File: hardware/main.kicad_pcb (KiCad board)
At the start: 2 copper layers, 5 parts, among them U1 SN74LVC245APW, U2 SN74LVC245APW, U3 SN74LVC245APW, U4 Z084000xP

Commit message: update pcb files
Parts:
- moved A1 58.3 mm to (62.6, 142.5), turned to -90 degrees
- moved U3 47.1 mm to (50.6, 118.2), turned to 180 degrees
- moved U1 46.1 mm to (78.0, 118.2)
- moved U2 43.9 mm to (64.5, 118.2)
- moved U4 32.4 mm to (85.5, 87.0), turned to -90 degrees
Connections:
- A1 pad 31: unconnected-(A1-GPIO26_ADC0-Pad31) -> IORQ
- A1 pad 32: KEYB -> WR
- A1 pad 34: unconnected-(A1-GPIO28_ADC2-Pad34)_1 -> KEYB
- U4 pad 20: unconnected-(U4-~{IORQ}-Pad20) -> IORQ
- U4 pad 22: unconnected-(U4-~{WR}-Pad22) -> WR
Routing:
- net +5V: track 0.00 -> 129.5 mm, vias 0 -> 4
- net CLK: track 0.00 -> 83.6 mm, vias 0 -> 1
- net IORQ: track 0.00 -> 79.5 mm
- net WR: track 0.00 -> 61.8 mm
- net GND: track 0.00 -> 54.6 mm, vias 0 -> 3
- net /B0: track 0.00 -> 51.9 mm, vias 0 -> 3
- net /B2: track 0.00 -> 51.5 mm, vias 0 -> 3
- net /B3: track 0.00 -> 51.5 mm, vias 0 -> 3
- net /B1: track 0.00 -> 50.6 mm, vias 0 -> 3
- net MREQ: track 0.00 -> 47.1 mm
- net /B7: track 15.1 -> 60.6 mm, vias 2 -> 3
- net /D3: track 0.00 -> 43.8 mm
- net /B6: track 16.1 -> 59.9 mm, vias 2 -> 3
- net DIR2: track 0.00 -> 43.4 mm, vias 0 -> 1
- net /D4: track 0.00 -> 40.4 mm, vias 0 -> 1
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- added copper zone on B.Cu, net GND
- added copper zone on F.Cu, net GND
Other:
- board outline added: 64 x 71.4 mm

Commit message: pcb routing
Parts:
- added C1: C_Small, Capacitor_SMD:C_0603_1608Metric_Pad1.08x0.95mm_HandSolder, F.Cu at (202.2, 95.3)
- added C2: C_Small, Capacitor_SMD:C_0603_1608Metric_Pad1.08x0.95mm_HandSolder, F.Cu at (190.9, 95.3)
- added C3: C_Small, Capacitor_SMD:C_0603_1608Metric_Pad1.08x0.95mm_HandSolder, F.Cu at (177.0, 95.0)
- added D1: LED_Small, LED_SMD:LED_0603_1608Metric_Pad1.05x0.95mm_HandSolder, F.Cu at (220.3, 125.7)
- added J2: Micro_SD_Card, Connector_PinSocket_2.54mm:PinSocket_1x08_P2.54mm_Horizontal, F.Cu at (161.3, 106.0)
- added R1: R_Small, Resistor_SMD:R_0603_1608Metric_Pad0.98x0.95mm_HandSolder, F.Cu at (155.3, 77.0)
- added R2: R_Small, Resistor_SMD:R_0603_1608Metric_Pad0.98x0.95mm_HandSolder, F.Cu at (202.7, 133.1)
- added R3: R_Small, Resistor_SMD:R_0603_1608Metric_Pad0.98x0.95mm_HandSolder, F.Cu at (186.6, 133.2)
- added R4: R_Small, Resistor_SMD:R_0603_1608Metric_Pad0.98x0.95mm_HandSolder, F.Cu at (175.2, 132.8)
- added R5: R_Small, Resistor_SMD:R_0603_1608Metric_Pad0.98x0.95mm_HandSolder, F.Cu at (168.2, 132.5)
- added R6: R_Small, Resistor_SMD:R_0603_1608Metric_Pad0.98x0.95mm_HandSolder, F.Cu at (150.9, 132.5)
- added R7: R_Small, Resistor_SMD:R_0603_1608Metric_Pad0.98x0.95mm_HandSolder, F.Cu at (181.3, 48.1)
- added R8: R_Small, Resistor_SMD:R_0603_1608Metric_Pad0.98x0.95mm_HandSolder, F.Cu at (186.5, 47.8)
- added R9: R_Small, Resistor_SMD:R_0603_1608Metric_Pad0.98x0.95mm_HandSolder, F.Cu at (191.0, 48.0)
- added SW1: SW_DIP_x01, Button_Switch_THT:SW_PUSH_6mm, F.Cu at (152.8, 71.0)
- added SW2: SW_DIP_x01, Button_Switch_THT:SW_PUSH_6mm, F.Cu at (148.5, 144.4)
- added SW3: SW_DIP_x01, Button_Switch_THT:SW_PUSH_6mm, F.Cu at (160.6, 144.4)
- added SW4: SW_DIP_x01, Button_Switch_THT:SW_PUSH_6mm, F.Cu at (172.7, 144.4)
- added SW5: SW_DIP_x01, Button_Switch_THT:SW_PUSH_6mm, F.Cu at (184.7, 144.4)
- added SW6: SW_DIP_x01, Button_Switch_THT:SW_PUSH_6mm, F.Cu at (196.8, 144.4)
- added SW7: SW_DIP_x01, Button_Switch_THT:SW_PUSH_6mm, F.Cu at (208.9, 144.4)
- moved A1 130.7 mm to (190.3, 114.8)
- moved U2 130.7 mm to (192.2, 90.5)
- moved U4 130.7 mm to (213.3, 59.3)
- moved U1 130.7 mm to (205.8, 90.5)
- moved U3 130.7 mm to (178.4, 90.5)
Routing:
- net +5V: track 129.5 -> 185.8 mm
- net GND: track 54.6 -> 108.2 mm
- net Net-(U4-~{RESET}): track 0.00 -> 49.8 mm
- net SEL1: track 18.0 -> 24.1 mm
- net /D1: track 36.3 -> 41.2 mm
- net SEL3: track 19.2 -> 21.8 mm
- net /B7: track 60.6 -> 62.9 mm
- net DIR1: track 23.5 -> 25.1 mm
- net /B6: track 59.9 -> 60.6 mm
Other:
- board size 64 x 71.4 mm -> 74.3 x 71.4 mm

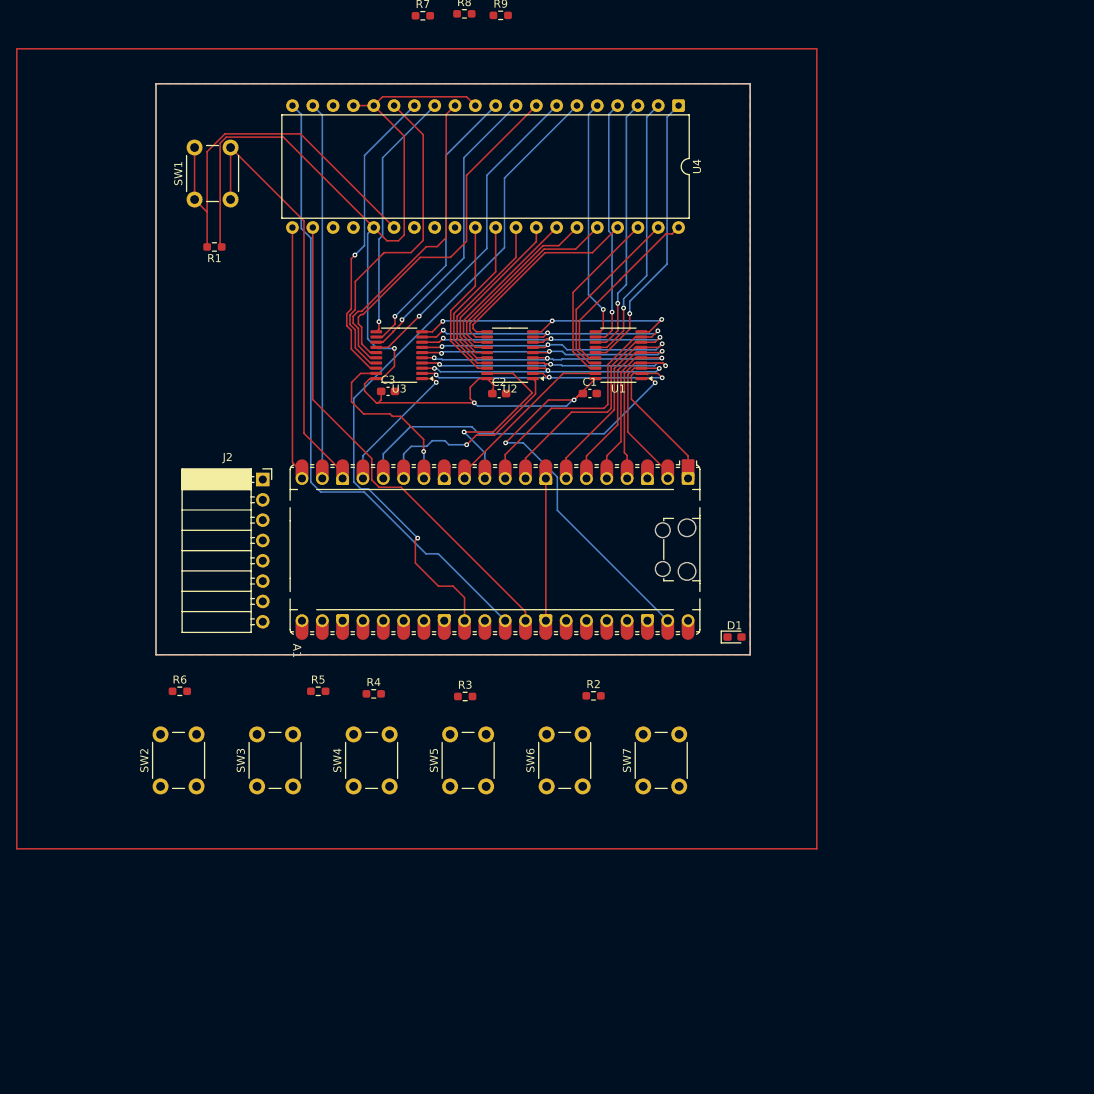
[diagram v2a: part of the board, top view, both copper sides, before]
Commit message: disable overclock, back to 150Mhz and add i2c display to schematic
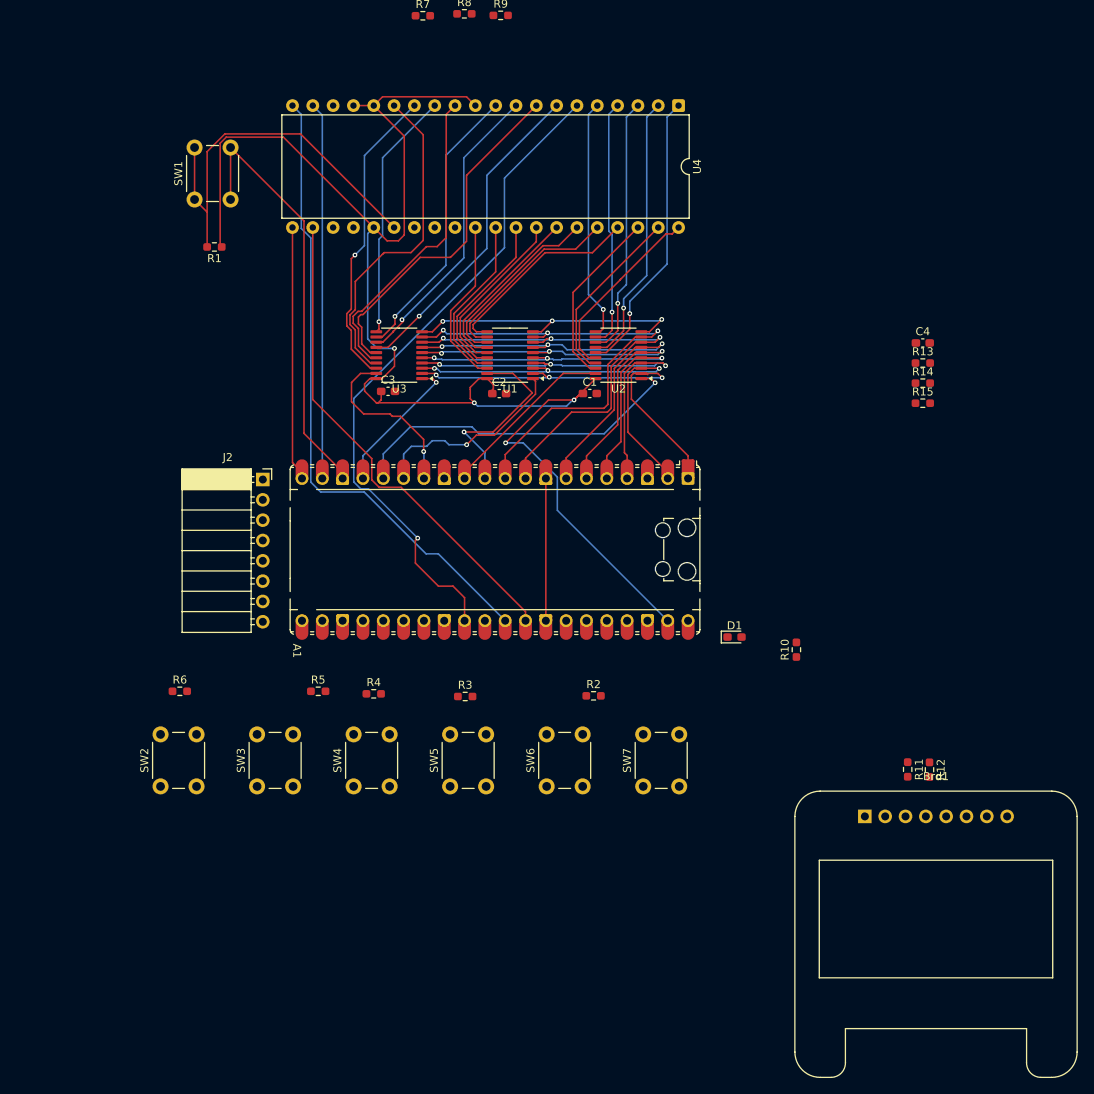
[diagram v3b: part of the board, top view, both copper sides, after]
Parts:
- added Brd1: SSD1306, Display:Adafruit_SSD1306_No_Mounting_Holes, F.Cu at (236.6, 148.1)
- added C4: C_Small, Capacitor_SMD:C_0603_1608Metric_Pad1.08x0.95mm_HandSolder, F.Cu at (243.8, 89.0)
- added R10: R_Small, Resistor_SMD:R_0603_1608Metric_Pad0.98x0.95mm_HandSolder, F.Cu at (228.0, 127.3)
- added R11: R_Small, Resistor_SMD:R_0603_1608Metric_Pad0.98x0.95mm_HandSolder, F.Cu at (241.9, 142.3)
- added R12: R_Small, Resistor_SMD:R_0603_1608Metric_Pad0.98x0.95mm_HandSolder, F.Cu at (244.7, 142.3)
- added R13: R_Small, Resistor_SMD:R_0603_1608Metric_Pad0.98x0.95mm_HandSolder, F.Cu at (243.8, 91.5)
- added R14: R_Small, Resistor_SMD:R_0603_1608Metric_Pad0.98x0.95mm_HandSolder, F.Cu at (243.8, 94.0)
- added R15: R_Small, Resistor_SMD:R_0603_1608Metric_Pad0.98x0.95mm_HandSolder, F.Cu at (243.8, 96.5)
- renumbered U2 to U1, U1 to U2
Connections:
- net Net-(U4-~{RESET}) renamed Z80_RES
- net RES renamed PICO_RES
- D1 pad 2: +5V -> Net-(D1-A)
- U4 pad 16: +5V -> Net-(U4-~{INT})
- U4 pad 17: +5V -> Net-(U4-~{NMI})
- U4 pad 25: +5V -> Net-(U4-~{BUSREQ})
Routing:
- removed copper zone on B.Cu, net GND
- removed copper zone on F.Cu, net GND
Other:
- board outline removed

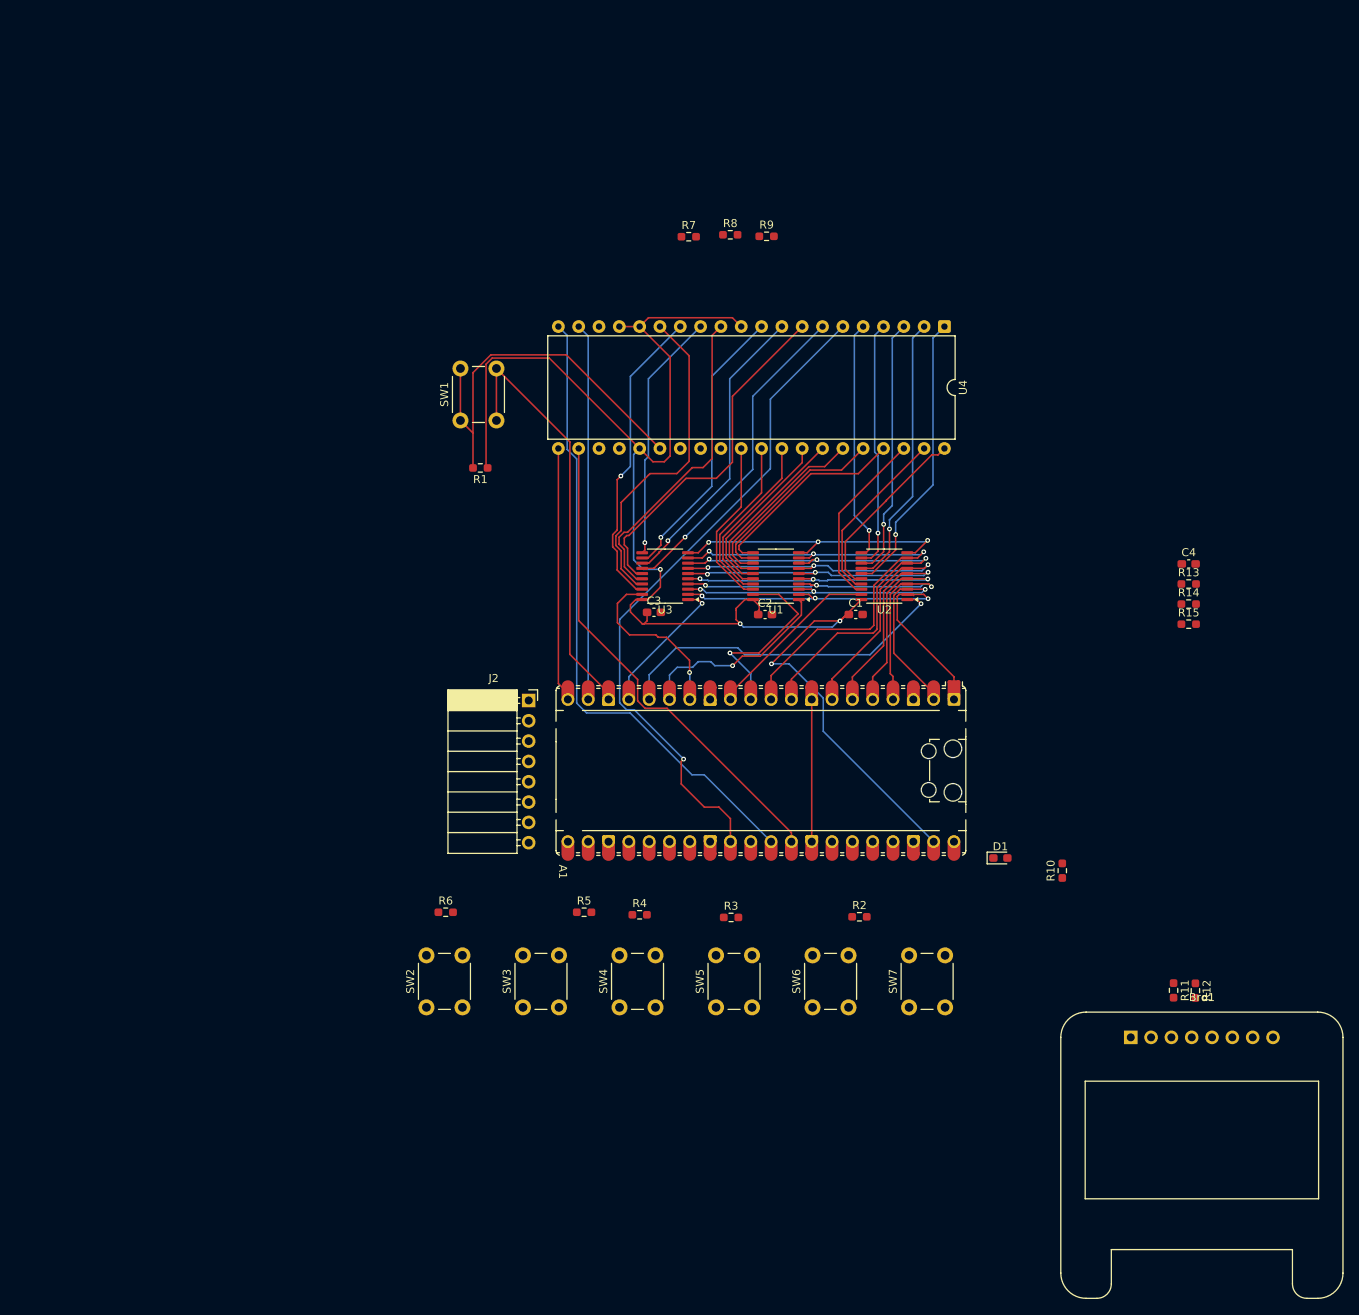
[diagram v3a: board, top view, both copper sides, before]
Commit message: use tht components
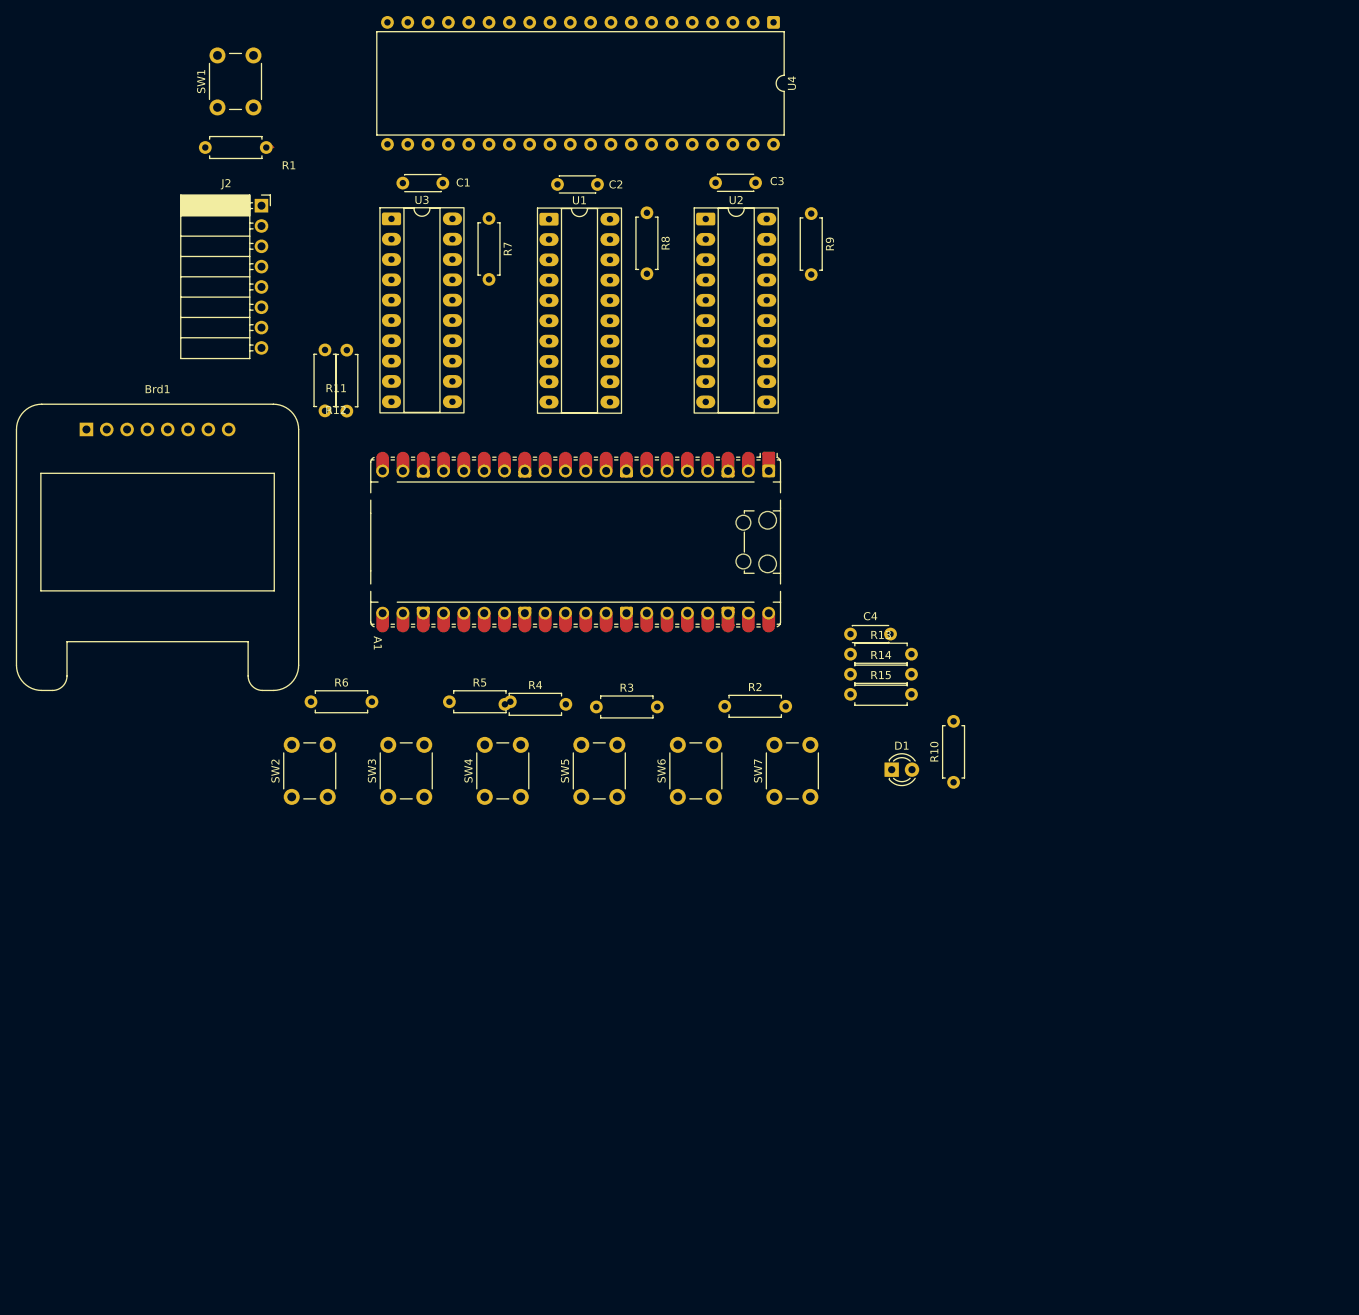
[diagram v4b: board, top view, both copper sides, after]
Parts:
- C1, C2, C3, C4: footprint Capacitor_SMD:C_0603_1608Metric_Pad1.08x0.95mm_HandSolder -> Capacitor_THT:C_Disc_D4.3mm_W1.9mm_P5.00mm
- D1: footprint LED_SMD:LED_0603_1608Metric_Pad1.05x0.95mm_HandSolder -> LED_THT:LED_D3.0mm
- R1, R10, R11, R12, R13, R14, R15, R2, R3, R4, R5, R6, R7, R8, R9: footprint Resistor_SMD:R_0603_1608Metric_Pad0.98x0.95mm_HandSolder -> Resistor_THT:R_Axial_DIN0207_L6.3mm_D2.5mm_P7.62mm_Horizontal
- U1, U2, U3: footprint Package_SO:TSSOP-20_4.4x6.5mm_P0.65mm -> Package_DIP:CERDIP-20_W7.62mm_SideBrazed_LongPads_Socket
- moved Brd1 151.0 mm to (106.0, 72.2)
- moved R12 130.7 mm to (135.8, 69.8), turned to 90 degrees
- moved R11 126.2 mm to (138.6, 69.9), turned to 90 degrees
- moved C1 74.6 mm to (150.6, 41.4), turned to 180 degrees
- moved J2 70.3 mm to (127.9, 44.2)
- moved C2 57.7 mm to (169.9, 41.5), turned to 180 degrees
- moved U3 56.2 mm to (144.2, 45.8), turned to 0 degrees
- moved C3 55.2 mm to (189.7, 41.3), turned to 180 degrees
- moved U1 52.9 mm to (163.8, 45.9), turned to 0 degrees
- moved U2 49.9 mm to (183.4, 45.9), turned to 0 degrees
- moved SW1 49.5 mm to (122.4, 31.9)
- moved R1 48.2 mm to (128.5, 36.9)
- moved U4 43.6 mm to (191.9, 21.3)
- moved C4 43.2 mm to (201.5, 97.7)
- moved R15 43.2 mm to (201.5, 105.3)
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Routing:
- net +5V: track 185.8 -> 0.28 mm, vias 4 -> 0
- net GND: track 108.2 -> 0.00 mm, vias 3 -> 0
- net CLK: track 83.6 -> 0.00 mm, vias 1 -> 0
- net IORQ: track 79.5 -> 0.00 mm
- net /B7: track 62.9 -> 0.00 mm, vias 3 -> 0
- net WR: track 61.8 -> 0.00 mm
- net /B6: track 60.6 -> 0.00 mm, vias 3 -> 0
- net /B5: track 55.4 -> 0.00 mm, vias 3 -> 0
- net /B4: track 53.5 -> 0.00 mm, vias 3 -> 0
- net /B0: track 51.7 -> 0.00 mm, vias 3 -> 0
- net /B2: track 51.6 -> 0.00 mm, vias 3 -> 0
- net /B3: track 51.3 -> 0.00 mm, vias 3 -> 0
- net /B1: track 50.5 -> 0.00 mm, vias 3 -> 0
- net Z80_RES: track 49.8 -> 0.00 mm
- net MREQ: track 47.1 -> 0.00 mm
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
